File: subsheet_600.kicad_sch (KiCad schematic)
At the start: 9 parts, among them U600 SIMM_30_PHY, U601 SIMM_30_PHY, U602 SIMM_30_PHY, U603 SIMM_30_PHY

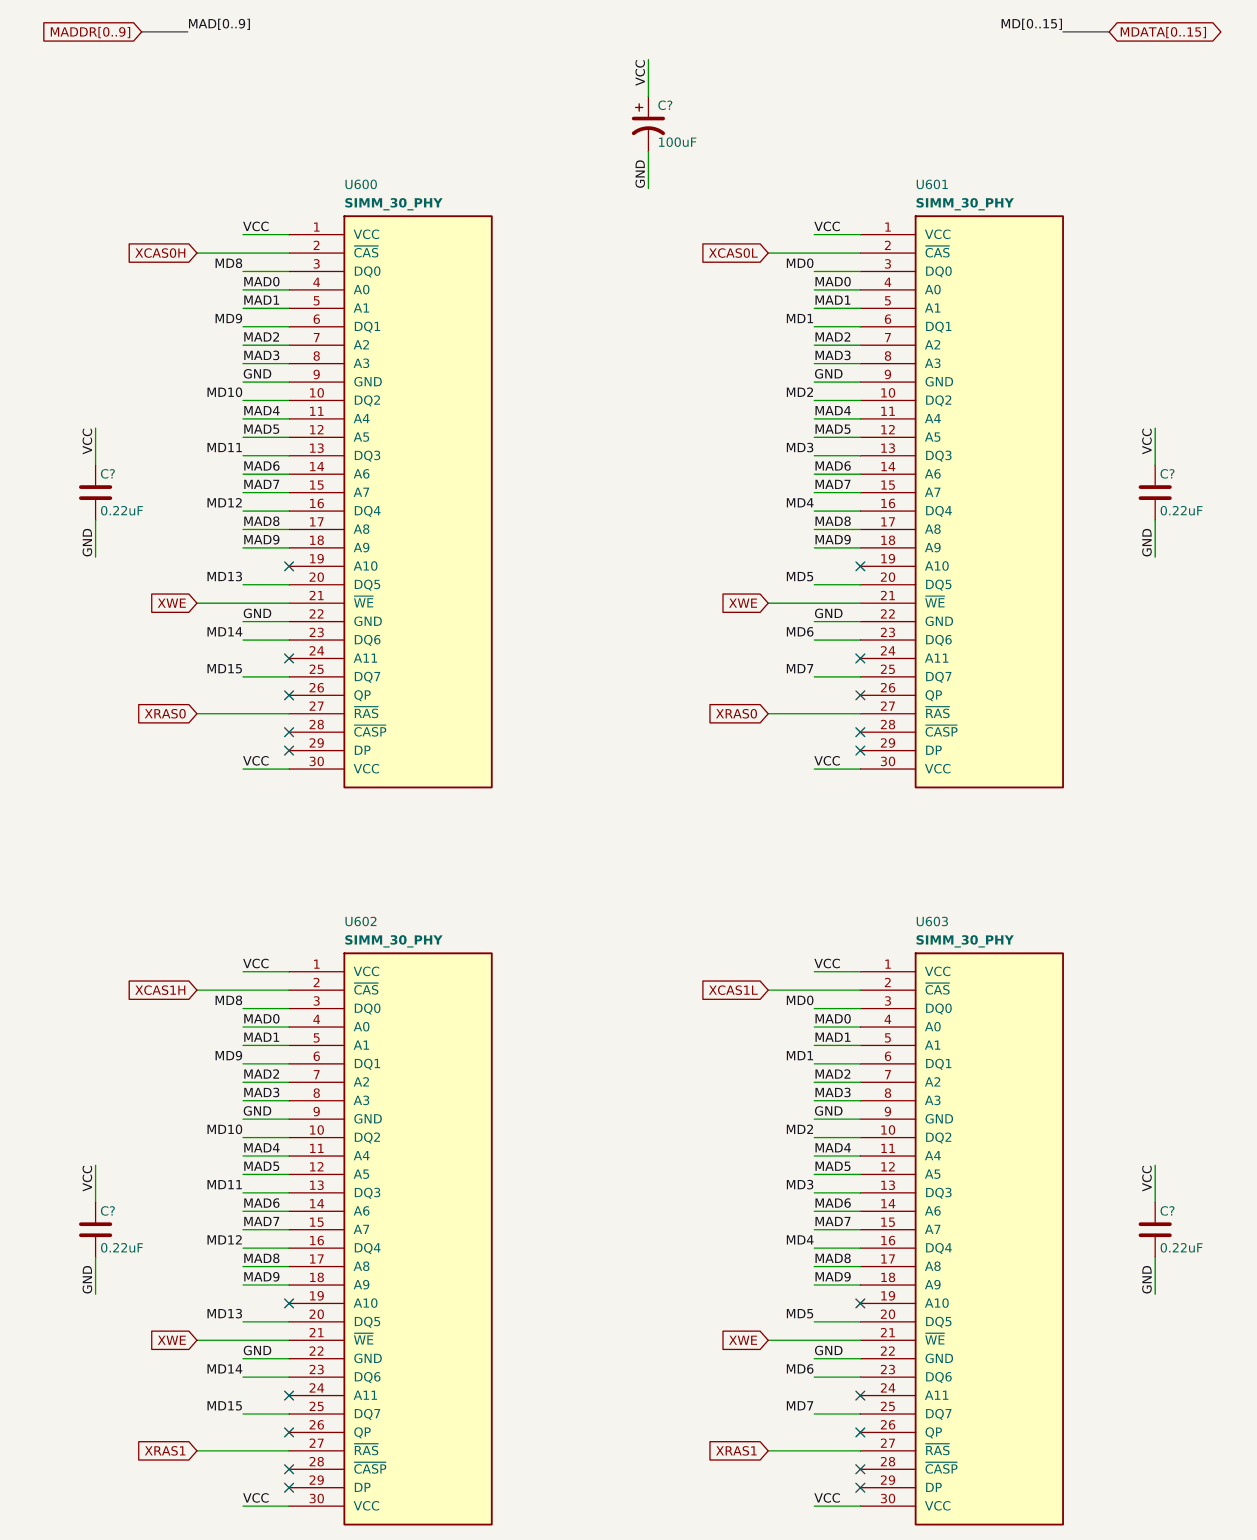
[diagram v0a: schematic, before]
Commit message: Resolves #3 : [schematic] annotate video port with signal name
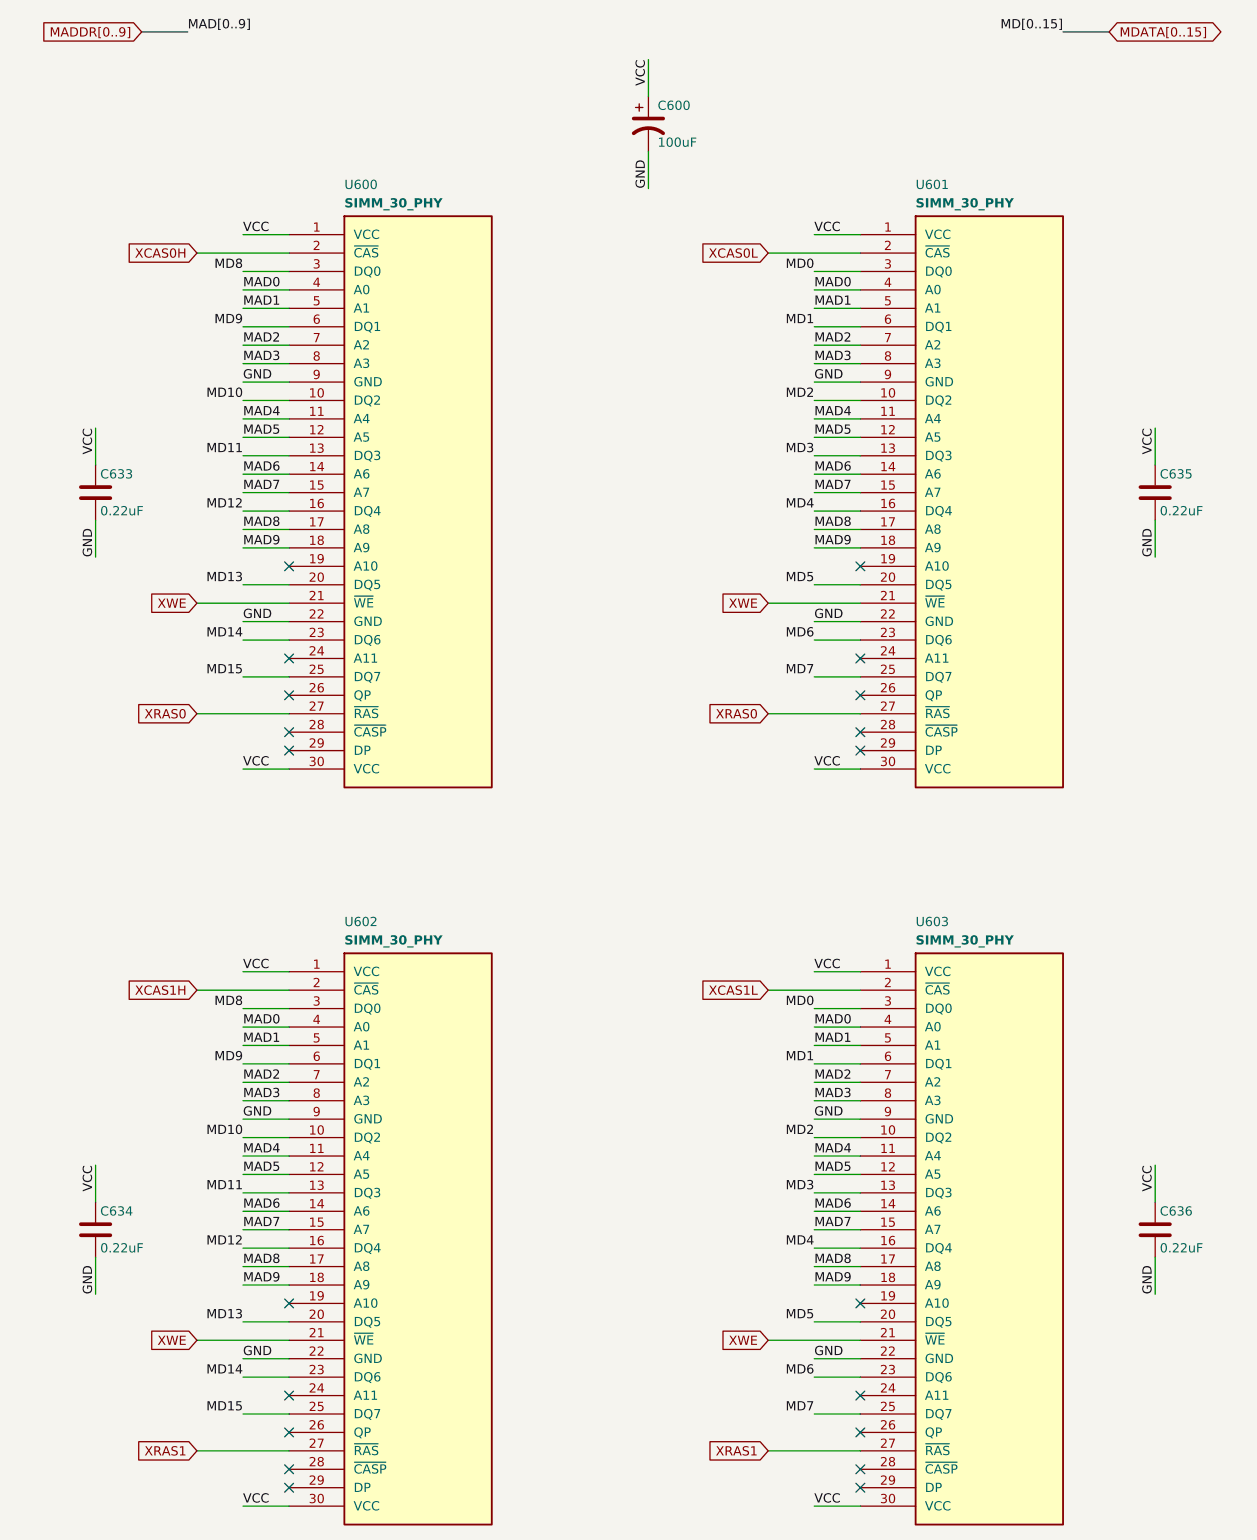
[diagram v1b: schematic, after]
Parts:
- gave numbers to parts that had none: 5
